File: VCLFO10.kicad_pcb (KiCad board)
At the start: 2 copper layers, 76 x 100 mm, 141 parts, among them J1 Conn_02x05_Odd_Even, Q1 BC547, Q2 BC547, U1 LM7805_TO220, U2 ED_VCLFO10, U3 TL072, U4 TL072, U5 LM358, U6 LM358, U7 LM358, U8 LM358

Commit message: Routing done
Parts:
- removed C4, C5: 10nF, Capacitor_SMD:C_1206_3216Metric_Pad1.33x1.80mm_HandSolder
- J_LFO_RANGE1, J_SYNC_MODE1: footprint Connector_PinSocket_2.54mm:PinSocket_1x05_P2.54mm_Horizontal -> My Stuff:PinSocket_1x05_P2.54mm_Horizontal_no_silkscreen
- moved R31 44.6 mm to (113.6, 64.5)
- moved R30 42.8 mm to (112.1, 94.5)
- moved R15 42.5 mm to (111.5, 73.5)
- moved R19 42.5 mm to (111.5, 71.2)
- moved R23 42.5 mm to (111.5, 68.8)
- moved R14 42.2 mm to (111.5, 101.9)
- moved R18 42.2 mm to (111.5, 99.6)
- moved R22 42.2 mm to (111.5, 97.2)
- moved R10 36.0 mm to (165.5, 146.7), turned to -90 degrees
- moved R27 34.8 mm to (103.3, 62.8), turned to 180 degrees
- moved R26 34.5 mm to (103.3, 91.3), turned to 180 degrees
- moved R7 27.5 mm to (163.4, 93.3), turned to 90 degrees
- moved C2 26.2 mm to (152.1, 72.0), turned to 0 degrees
- moved C10 25.0 mm to (160.8, 93.2), turned to 90 degrees
- moved C3 23.8 mm to (158.2, 72.0)
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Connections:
- RV_LFO_RANGE1 pad 1: Net-(RV_LFO_RANGE1-Pad1) -> GND
- RV_LFO_RANGE1 pad MP: Net-(RV_LFO_RANGE1-Pad1) -> GND
- RV_SYNC_MODE1 pad 1: Net-(RV_SYNC_MODE1-Pad1) -> GND
- RV_SYNC_MODE1 pad MP: Net-(RV_SYNC_MODE1-Pad1) -> GND
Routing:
- net +12V: track 0.00 -> 285.3 mm, vias 0 -> 5
- net -12V: track 0.00 -> 272.6 mm, vias 0 -> 2
- net +5V: track 0.00 -> 157.8 mm, vias 0 -> 3
- net Net-(J_FREQ1-PadT): track 0.00 -> 152.8 mm, vias 0 -> 2
- net Net-(J_STEP_RATE1-PadT): track 0.00 -> 107.2 mm, vias 0 -> 1
- net Net-(J_WAVE_DISTORT1-PadT): track 0.00 -> 86.6 mm, vias 0 -> 1
- net Net-(C11-Pad1): track 0.00 -> 79.6 mm, vias 0 -> 2
- net /Outputs/TO_OUT: track 0.00 -> 74.2 mm, vias 0 -> 4
- net /Inputs/LEVEL_CV: track 0.00 -> 64.1 mm, vias 0 -> 3
- net Net-(RV_ZERO_ADJUST1-Pad2): track 0.00 -> 63.6 mm, vias 0 -> 1
- net /Inputs/SYNC_MODE_CV: track 0.00 -> 61.3 mm, vias 0 -> 1
- net /Inputs/SYNC_IN: track 0.00 -> 56.3 mm, vias 0 -> 2
- net /Inputs/FREQ_CV: track 0.00 -> 54.3 mm, vias 0 -> 1
- net /Inputs/LFO_RANGE: track 0.00 -> 53.3 mm, vias 0 -> 2
- net Net-(J_LEVEL1-PadT): track 0.00 -> 50.6 mm, vias 0 -> 1
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
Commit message: Geographic reannotate and silkscreen cleanup
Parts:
- renumbered C13 to C1, C16 to C10, C10 to C11, C17 to C12, C20 to C13, C11 to C14, C9 to C15, C22 to C16, C8 to C17, C23 to C18, C15 to C19, C19 to C2, C14 to C20, C12 to C3, C18 to C4, C1 to C5, C3 to C6, C2 to C7, C6 to C8, C7 to C9, D6 to D10, D7 to D2, D10 to D3, D3 to D6, D2 to D7, D9 to D8, D8 to D9, FB2 to FB1, FB1 to FB2, Q2 to Q1, Q1 to Q2, R65 to R1, R57 to R10, R53 to R11, R41 to R12, R60 to R13, R56 to R14, R61 to R15, R64 to R16, R27 to R17, R31 to R18, R45 to R19, R70 to R2, R37 to R20, R23 to R21, R19 to R22, R15 to R23, R67 to R24, R39 to R25, R51 to R26, R43 to R27, R47 to R28, R26 to R29, R73 to R3, R7 to R30, R8 to R31, R9 to R32, R30 to R33, R59 to R34, R63 to R35, R22 to R36, R17 to R37, R55 to R38, R72 to R39, R49 to R4, R21 to R40, R18 to R41, R28 to R42, R14 to R43, R32 to R44, R25 to R45, R24 to R46, R29 to R47, R20 to R48, R16 to R49, R68 to R5, R46 to R50, R74 to R51, R38 to R52, R75 to R53, R4 to R54, R5 to R55, R6 to R56, R71 to R57, R54 to R58, R50 to R59, R40 to R6, R42 to R60, R76 to R61, R58 to R62, R36 to R63, R3 to R64, R69 to R65, R62 to R66, R66 to R67, R12 to R68, R13 to R69, R48 to R7, R2 to R70, R35 to R71, R11 to R72, R10 to R73, R52 to R8, R44 to R9, U5 to U1, U8 to U2, U1 to U3, U2 to U4, U7 to U5, U3 to U6, U4 to U7, U6 to U8
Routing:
- net Net-(C14-Pad1): track 79.6 -> 82.0 mm, vias 2 -> 4

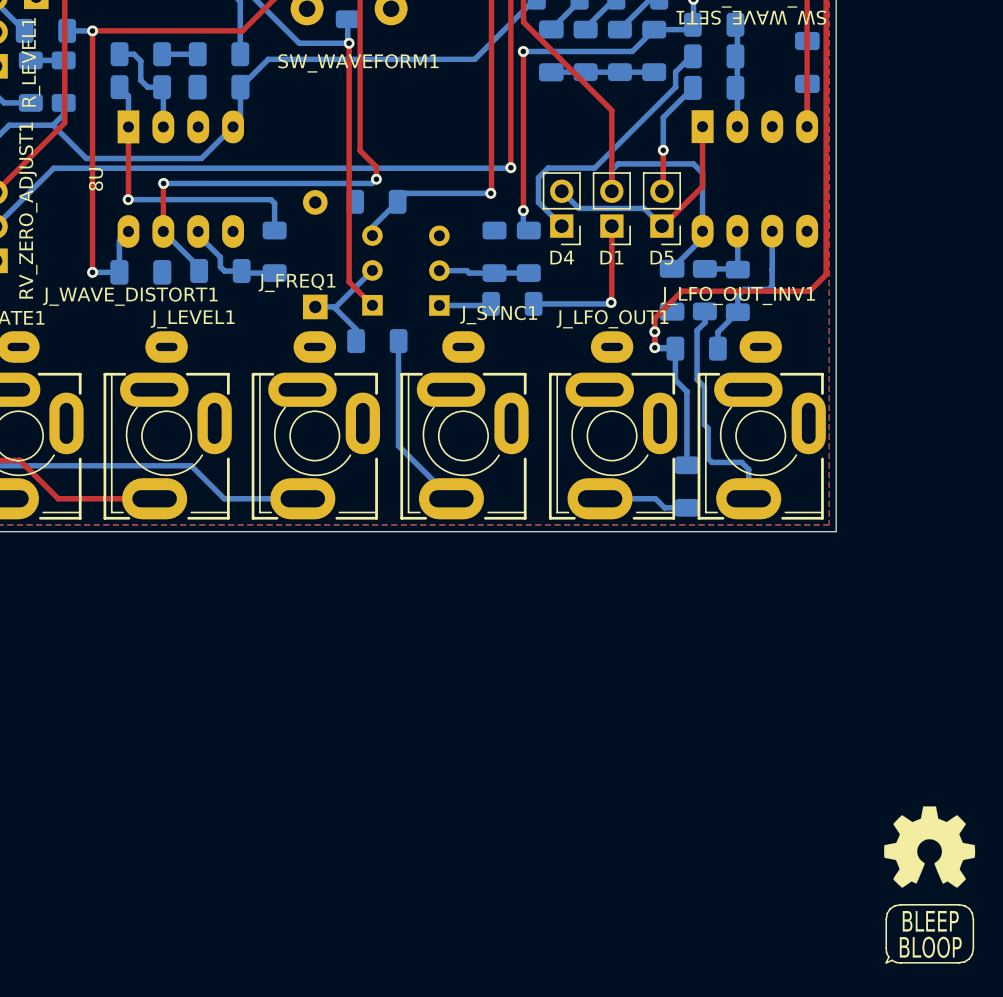
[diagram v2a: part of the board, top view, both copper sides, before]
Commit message: Added a help text on silkscreen
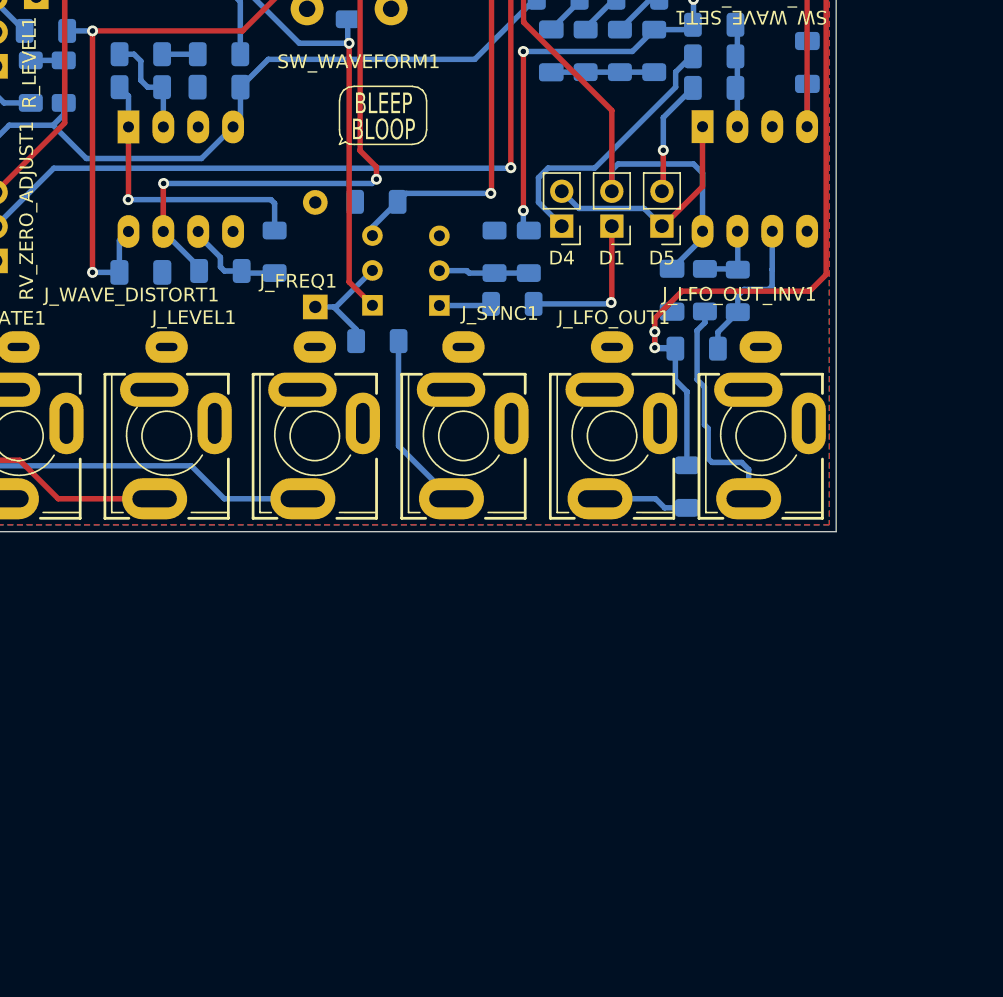
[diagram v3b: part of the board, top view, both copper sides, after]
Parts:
- LOGO3: moved to B.Cu
- moved LOGO3 88.5 mm to (124.7, 106.7), turned to 180 degrees
- moved LOGO2 71.7 mm to (143.4, 119.7)
- moved LOGO1 71.7 mm to (143.3, 119.7)
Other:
- board text added: "BC547"
- board text added: "ED VCLFO10"
- board text added: "FREQ"
- board text added: "INV. LFO"
- board text added: "LEVEL"
- board text added: "LFO"
- board text added: "LM358"
- board text added: "RED"
- board text added: "RobotDialogs VCLFO10 v1.0 June 2022"
- board text added: "STEP RATE"
- board text added: "STEPRATE"
- board text added: "SYNC"
- board text added: "TL072"
- board text added: "WAVE DISTORT"
- board text added: "WAVE SMOOTH"
- board text added: "WAVESET"
- board text added: "ZERO ADJUST"
